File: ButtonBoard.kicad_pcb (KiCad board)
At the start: 2 copper layers, 27.2 x 22.4 mm, 4 parts, among them J1 Conn_01x06_Male

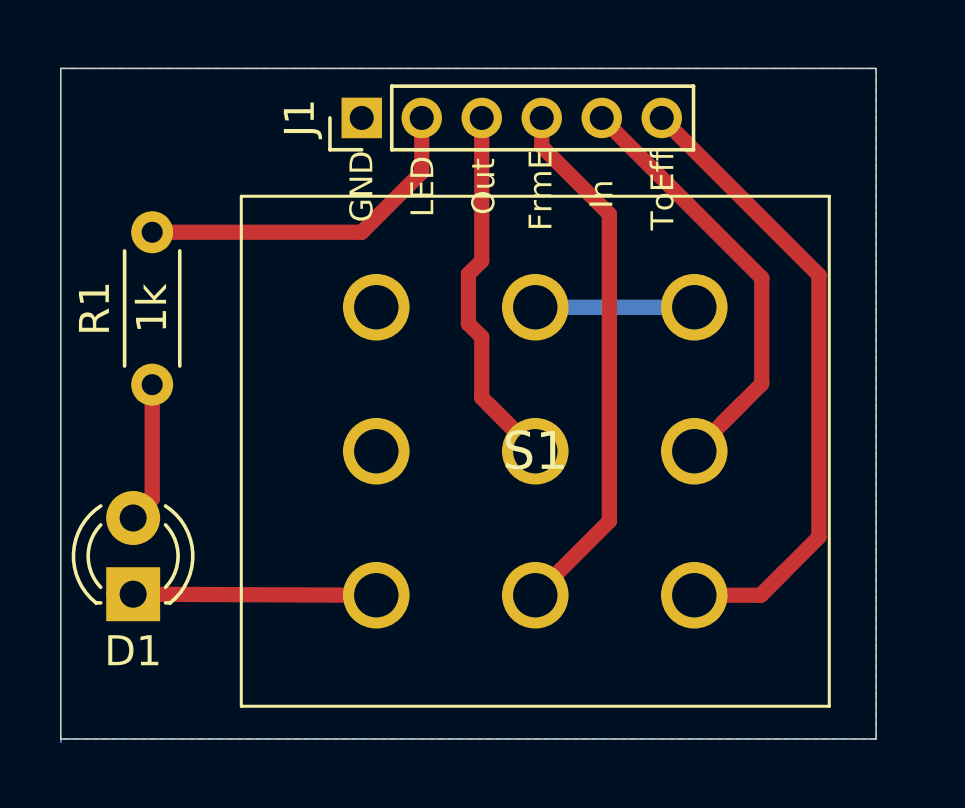
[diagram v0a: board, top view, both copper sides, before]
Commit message: rearrange and plot for build
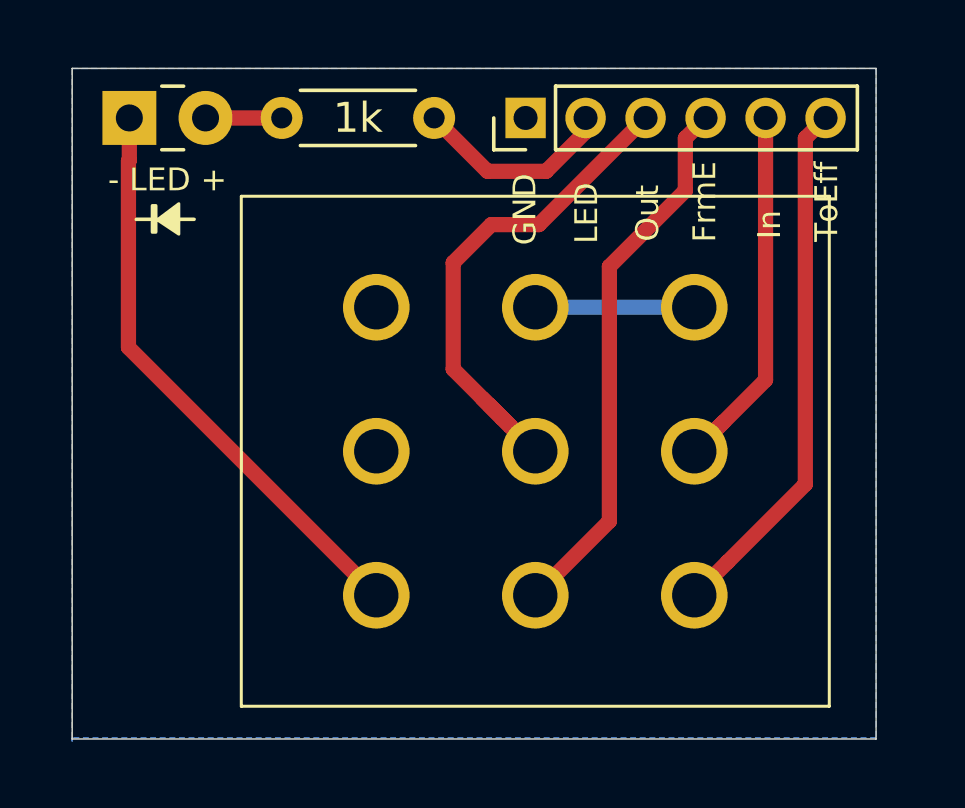
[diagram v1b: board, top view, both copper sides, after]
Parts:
- D1: value LED -> - LED +; footprint LED_THT:LED_D3.0mm -> LEDs:LED_Rectangular_W3.0mm_H2.0mm
- moved D1 15.9 mm to (74.2, 48.9), turned to 0 degrees
- moved R1 10.1 mm to (84.3, 48.9), turned to 180 degrees
- moved J1 5.46 mm to (87.4, 48.9)
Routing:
- net Net-(D1-Pad1): track 8.74 -> 19.3 mm
- net Ouput: track 13.3 -> 19.4 mm
- net Net-(J1-Pad2): track 11.6 -> 6.79 mm
- net ToEffect: track 22.2 -> 17.7 mm
- net Net-(D1-Pad2): track 4.71 -> 2.54 mm
- net Input: track 15.1 -> 13.5 mm
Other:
- board size 27.2 x 22.4 mm -> 26.8 x 22.4 mm

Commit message: fix pin size bump version to 1.1
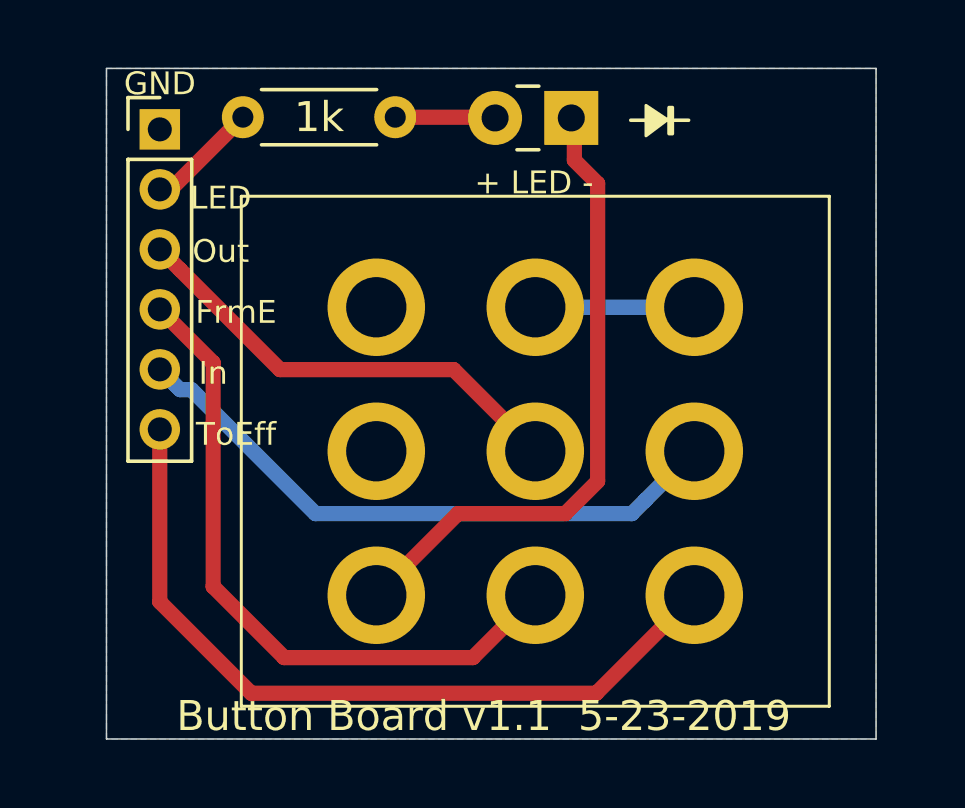
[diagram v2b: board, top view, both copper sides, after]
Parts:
- D1: value - LED + -> + LED -
- moved D1 14.7 mm to (88.9, 48.9), turned to 180 degrees
- moved J1 12.2 mm to (75.2, 49.3), turned to 0 degrees
- moved R1 6.38 mm to (78.0, 48.9), turned to 0 degrees
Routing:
- net Input: track 13.5 -> 22.0 mm
- net ToEffect: track 17.7 -> 26.2 mm
- net FromEffect: track 18.3 -> 22.6 mm
- net Ouput: track 19.4 -> 15.3 mm
- net Net-(J1-Pad2): track 6.79 -> 3.77 mm
- net Net-(D1-Pad1): track 19.3 -> 21.4 mm
- net Net-(D1-Pad2): track 2.54 -> 3.44 mm
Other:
- board size 26.8 x 22.4 mm -> 25.7 x 22.4 mm
- board text added: "Button Board v1.1 5-23-2019"

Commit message: Bump to version 1.2 make the holes a little bigger
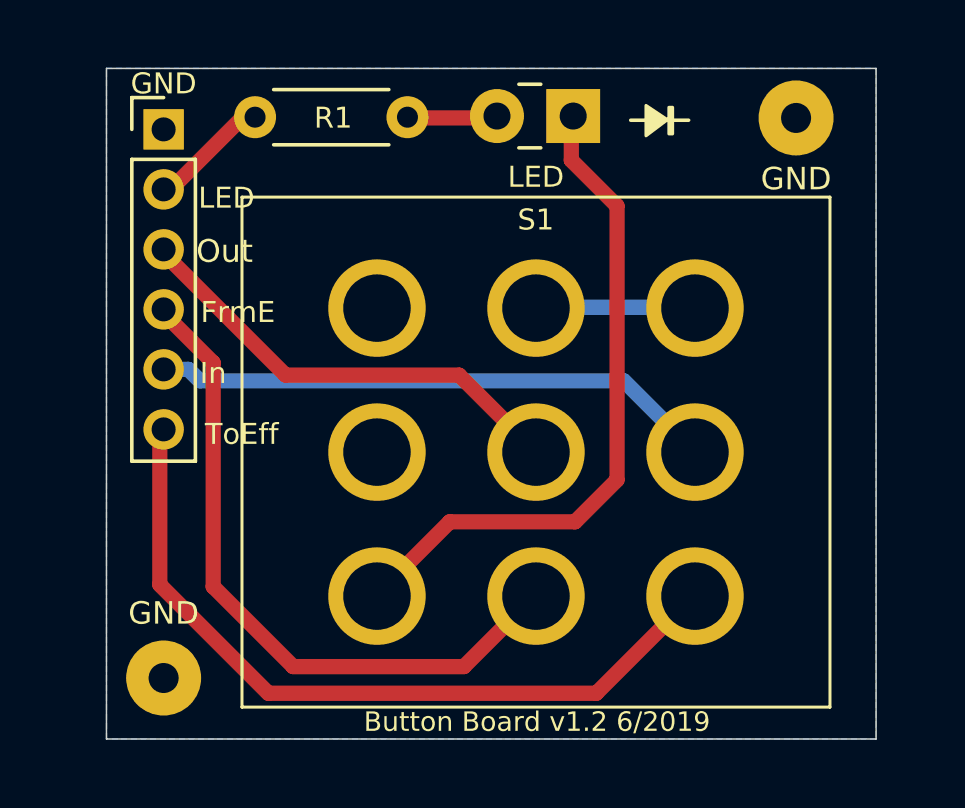
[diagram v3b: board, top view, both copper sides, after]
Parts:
- added GND: MountingHole_Pad, Wire_Pads:SolderWirePad_single_1mmDrill, F.Cu at (75.3, 67.6)
- added GND: MountingHole_Pad, Wire_Pads:SolderWirePad_single_1mmDrill, F.Cu at (96.4, 48.9)
- D1: value + LED - -> LED
- S1: footprint SF17020F-0302-21R-L-015:SF17020F030221RL015 -> Footswitch:Footswitch_3PDT
- moved R1 0.41 mm to (78.4, 48.9)
- moved J1 0.13 mm to (75.3, 49.3)
- moved D1 0.09 mm to (89.0, 48.8)
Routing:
- net Input: track 22.0 -> 20.3 mm
- net Net-(D1-Pad1): track 21.4 -> 22.3 mm
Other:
- board text added: "Button Board v1.2 6/2019"
- board text removed: "Button Board v1.1 5-23-2019"

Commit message: re arrange some pins and ground the toEffect pin when bypassed
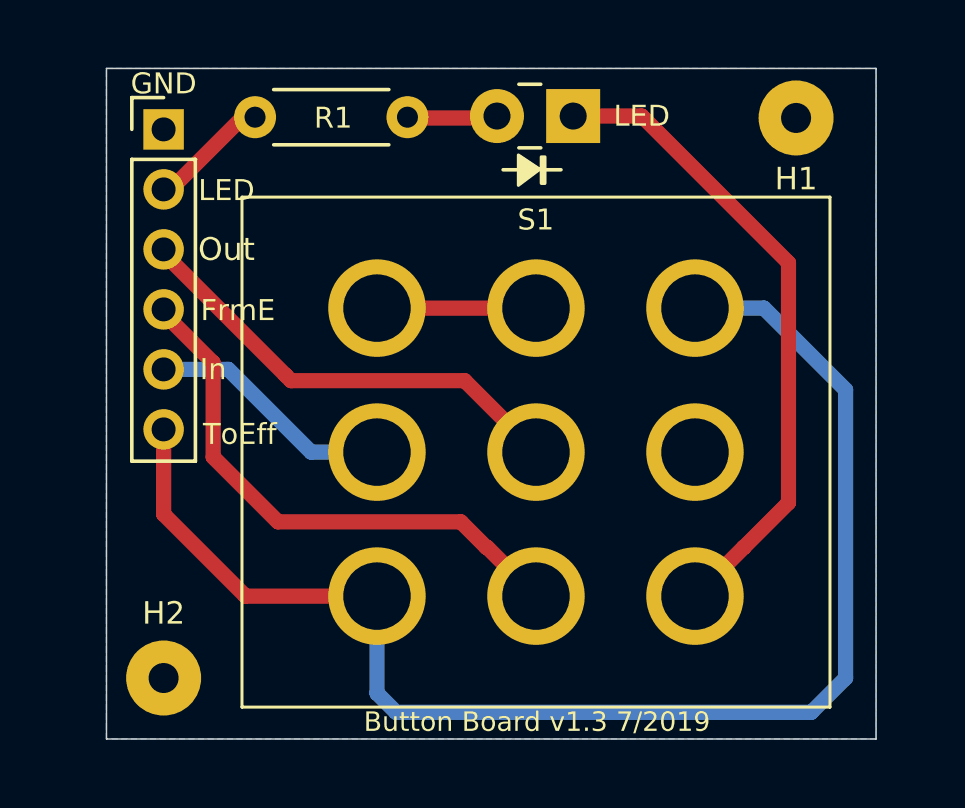
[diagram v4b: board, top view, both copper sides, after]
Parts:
- renumbered GND to H1, GND to H2
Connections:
- net Ouput renamed Output
- S1 pad 1: ToEffect -> Net-(D1-Pad1)
- S1 pad 2: Input -> GND
- S1 pad 3: Net-(S1-Pad3) -> ToEffect
- S1 pad 6: Net-(S1-Pad3) -> Net-(S1-Pad6)
- S1 pad 7: Net-(D1-Pad1) -> ToEffect
- S1 pad 8: GND -> Input
- S1 pad 9: (no net) -> Net-(S1-Pad6)
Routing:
- net ToEffect: track 25.8 -> 46.4 mm
- net Input: track 20.3 -> 8.25 mm
- net Net-(S1-Pad6): track 0.00 -> 5.30 mm
- net Net-(S1-Pad3): track 5.30 -> 0.00 mm
- net FromEffect: track 22.8 -> 18.3 mm
- net GND: track 0.00 -> 1.36 mm
- net Net-(D1-Pad1): track 22.3 -> 21.6 mm
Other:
- board text added: "Button Board v1.3 7/2019"
- board text removed: "Button Board v1.2 6/2019"

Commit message: update board with better connector
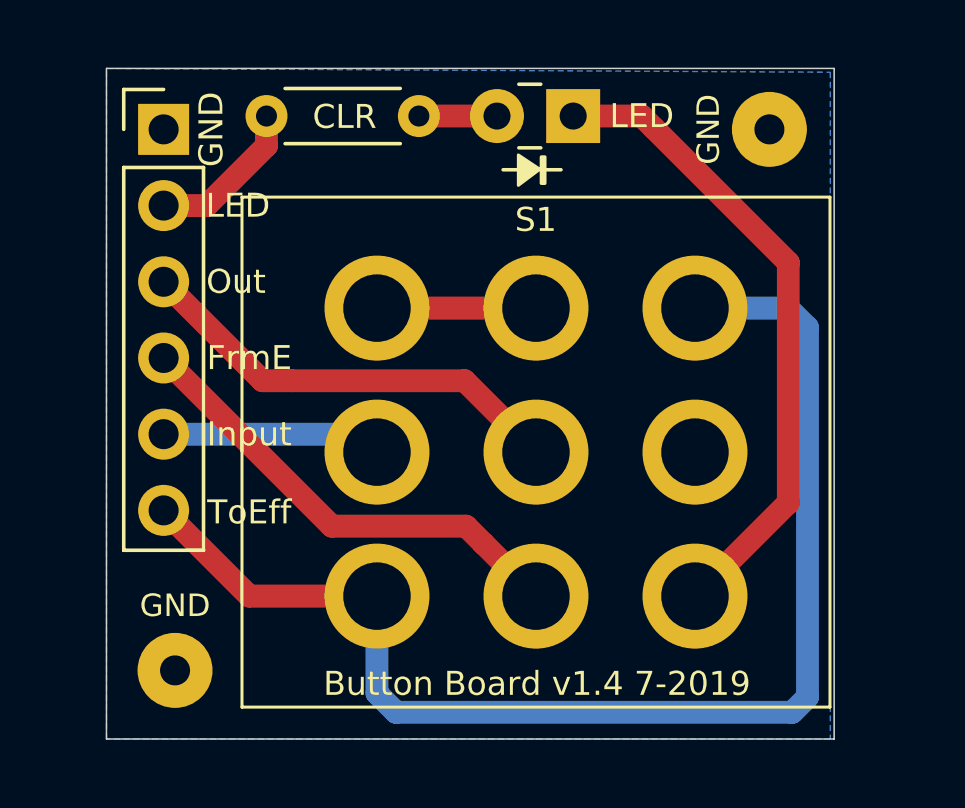
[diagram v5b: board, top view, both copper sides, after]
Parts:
- J1: value Conn_01x06_Male -> GND; footprint Connector_PinHeader_2.00mm:PinHeader_1x06_P2.00mm_Vertical -> Connector_PinHeader_2.54mm:PinHeader_1x06_P2.54mm_Vertical
- moved GND 0.97 mm to (95.5, 49.3)
- moved GND 0.46 mm to (75.7, 67.3)
- moved CLR 0.38 mm to (78.7, 48.8)
- renumbered R1 to CLR, H2 to GND, H1 to GND
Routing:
- net Output: track 15.3 -> 23.9 mm
- net ToEffect: track 46.4 -> 42.7 mm
- net FromEffect: track 18.3 -> 15.7 mm
- net Net-(J1-Pad2): track 3.77 -> 5.61 mm
- net Input: track 8.25 -> 7.36 mm
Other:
- board size 25.7 x 22.4 mm -> 24.3 x 22.4 mm
- board text added: "Button Board v1.4 7-2019"
- board text added: "Input"
- board text removed: "Button Board v1.3 7/2019"
- board text removed: "In"
